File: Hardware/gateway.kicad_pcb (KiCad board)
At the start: 2 copper layers, 65 x 56 mm, 27 parts, among them J0 Raspberry_Pi_2_3_40HAT, J1 CONN_01X02, J2 Conn_Coaxial, J3 Conn_Coaxial, U0 CAT24C32, U0a1 DRF1278F, U0b1 XL1278-SMT, U0c1 RFM9xW-xxxS2, U1a1 DRF1278F, U1b1 XL1278-SMT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

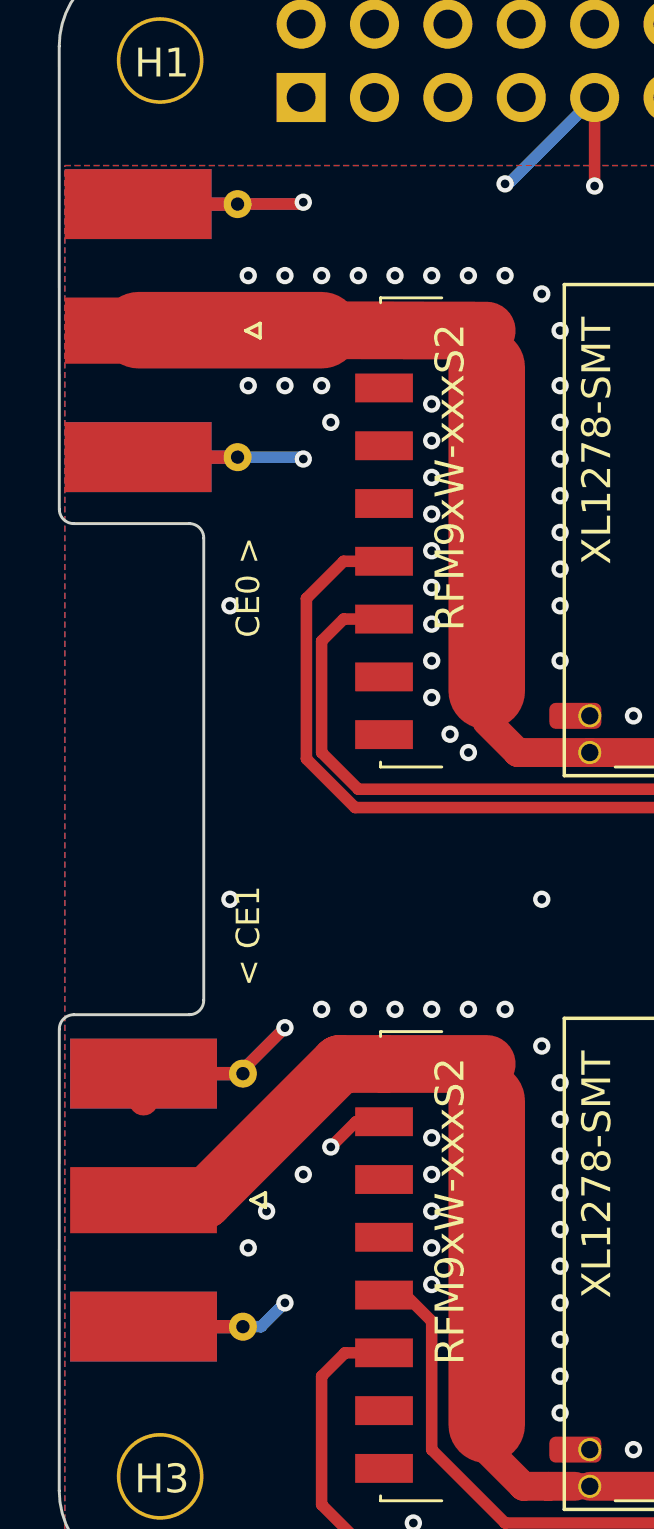
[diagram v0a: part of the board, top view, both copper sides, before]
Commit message: Fix antenna ground connections
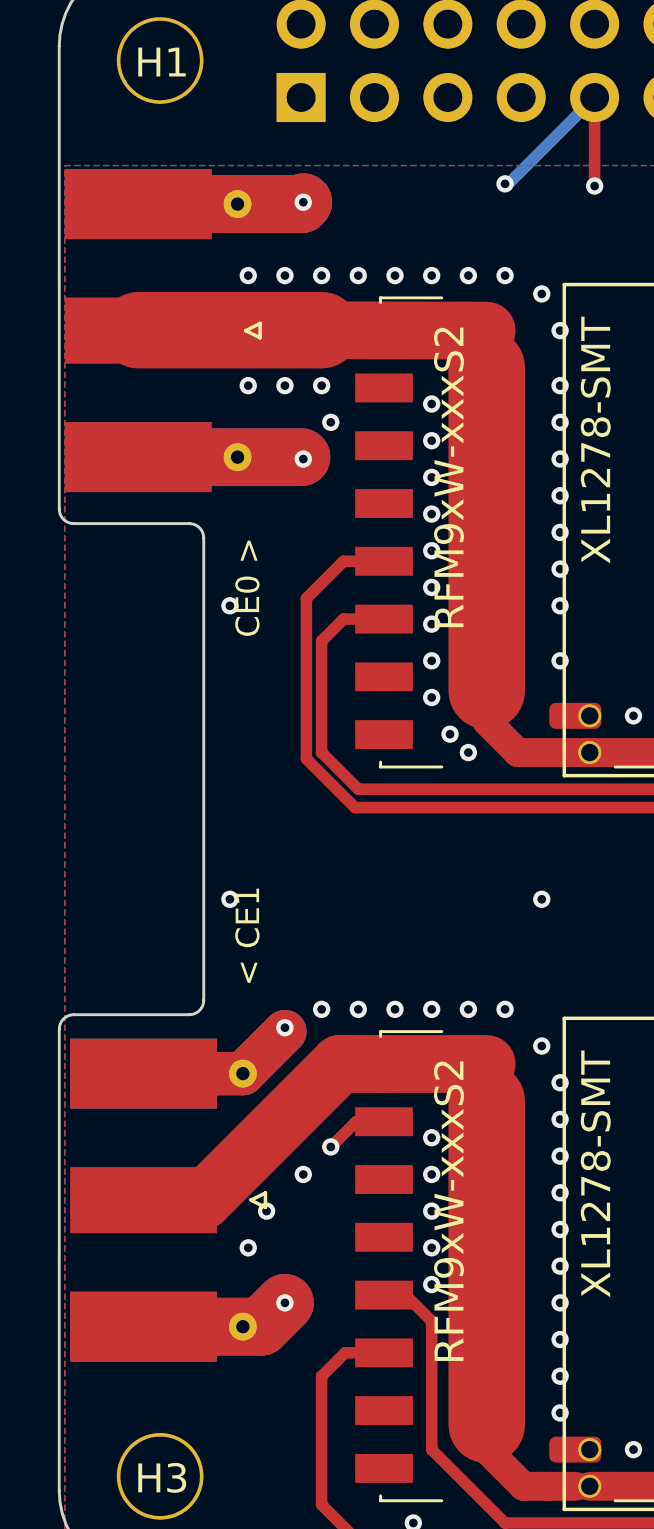
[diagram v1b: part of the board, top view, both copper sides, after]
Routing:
- net GND: track 56.1 -> 86.3 mm
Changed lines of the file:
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@@
     (thickness 1.6002)
     (drawings 32)
-    (tracks 431)
+    (tracks 436)
     (zones 0)
     (modules 27)
@@
   )
   (setup
-    (last_trace_width 0.6)
+    (last_trace_width 0.127)
     (user_trace_width 0.15)
     (user_trace_width 0.2)
@@
     (visible_elements 7FFFFE3F)
     (pcbplotparams
-      (layerselection 0x010f8_80000007)
+      (layerselection 0x010f0_ffffffff)
       (usegerberextensions false)
       (usegerberattributes false)
@@
       (plotinvisibletext false)
       (padsonsilk true)
-      (subtractmaskfromsilk false)
+      (subtractmaskfromsilk true)
       (outputformat 1)
       (mirror false)
       (drillshape 0)
       (scaleselection 1)
-      (outputdirectory "prod"))
+      (outputdirectory "Gerber/"))
   )
   (net 0 "")
@@
   (gr_line (start 81.546356 116.817611) (end 140.546356 116.817611) (layer Edge.Cuts) (width 0.1))
   (gr_arc (start 140.546356 113.817611) (end 140.546356 116.817611) (angle -89.9) (layer Edge.Cuts) (width 0.1))
-  (segment (start 81.48 100.315) (end 81.465 100.33) (width 1) (layer Front) (net 1) (status 30))
   (segment (start 105.79 113.045) (end 104.155 113.045) (width 0.4) (layer Front) (net 1) (status 10))
   (segment (start 103.505 112.395) (end 102.381 112.395) (width 0.4) (layer Front) (net 1) (status 20))
@@
   (via (at 86.995 78.105) (size 0.6) (drill 0.3) (layers Front Back) (net 1))
   (via (at 86.36 97.79) (size 0.6) (drill 0.3) (layers Front Back) (net 1))
-  (segment (start 84.905 99.245) (end 86.36 97.79) (width 0.4) (layer Front) (net 1) (status 10))
-  (segment (start 84.905 99.379) (end 84.905 99.245) (width 0.4) (layer Front) (net 1) (status 30))
-  (segment (start 86.93 69.28) (end 86.995 69.215) (width 0.4) (layer Back) (net 1))
-  (segment (start 84.72 69.28) (end 86.93 69.28) (width 0.4) (layer Back) (net 1) (status 10))
-  (segment (start 86.93 78.04) (end 86.995 78.105) (width 0.4) (layer Back) (net 1))
-  (segment (start 84.72 78.04) (end 86.93 78.04) (width 0.4) (layer Back) (net 1) (status 10))
-  (segment (start 84.455 99.379) (end 84.771 99.379) (width 0.4) (layer Back) (net 1) (status 30))
-  (segment (start 84.905 99.245) (end 86.36 97.79) (width 0.4) (layer Back) (net 1) (status 10))
-  (segment (start 84.905 99.379) (end 84.905 99.245) (width 0.4) (layer Back) (net 1) (status 30))
-  (segment (start 84.72 69.28) (end 86.93 69.28) (width 0.4) (layer Front) (net 1) (status 10))
-  (segment (start 81.465 99.379) (end 84.905 99.379) (width 0.4) (layer Front) (net 1) (status 30))
+  (segment (start 84.72 69.28) (end 86.93 69.28) (width 2) (layer Back) (net 1) (status 10))
+  (segment (start 81.465 99.379) (end 84.905 99.379) (width 1.5) (layer Front) (net 1) (status 30))
   (via (at 93.98 68.58) (size 0.6) (drill 0.3) (layers Front Back) (net 1))
   (segment (start 94.09 68.58) (end 93.98 68.58) (width 0.4) (layer Back) (net 1))
@@
   (segment (start 105.79 99.045) (end 106.06 99.045) (width 0.4) (layer Front) (net 1) (status 30))
   (segment (start 117.4 65.965) (end 117.4 65.59) (width 0.4) (layer Back) (net 1) (status 30))
-  (segment (start 84.905 108.139) (end 85.536 108.139) (width 0.4) (layer Back) (net 1) (status 10))
   (segment (start 135.18 65.59) (end 137.795 68.205) (width 0.4) (layer Front) (net 1) (status 10))
   (segment (start 117.4 65.59) (end 117.4 68.505) (width 0.4) (layer Front) (net 1) (status 10))
@@
   (segment (start 112.13 99.695) (end 110.49 99.695) (width 0.4) (layer Front) (net 1) (status 10))
   (segment (start 88.82 101.045) (end 87.9475 101.9175) (width 0.4) (layer Front) (net 1) (status 10))
-  (segment (start 85.536 108.139) (end 86.36 107.315) (width 0.4) (layer Back) (net 1))
   (segment (start 97.08 65.59) (end 97.08 68.655) (width 0.4) (layer Front) (net 1) (status 10))
   (segment (start 137.795 68.205) (end 137.795 68.58) (width 0.4) (layer Front) (net 1))
@@
   (via (at 90.805 114.935) (size 0.6) (drill 0.3) (layers Front Back) (net 1))
   (via (at 116.205 104.14) (size 0.6) (drill 0.3) (layers Front Back) (net 1))
+  (segment (start 86.93 78.04) (end 86.995 78.105) (width 0.127) (layer Front) (net 1))
+  (segment (start 81.28 78.04) (end 86.93 78.04) (width 2) (layer Front) (net 1))
+  (segment (start 86.93 69.28) (end 86.995 69.215) (width 2) (layer Front) (net 1))
+  (segment (start 81.28 69.28) (end 86.93 69.28) (width 2) (layer Front) (net 1))
+  (segment (start 85.536 108.139) (end 86.36 107.315) (width 2) (layer Front) (net 1))
+  (segment (start 81.465 108.139) (end 85.536 108.139) (width 2) (layer Front) (net 1))
+  (segment (start 85.536 108.139) (end 86.36 107.315) (width 2) (layer Back) (net 1))
+  (segment (start 81.465 108.139) (end 85.536 108.139) (width 2) (layer Back) (net 1))
+  (segment (start 81.465 99.379) (end 84.905 99.379) (width 1.5) (layer Back) (net 1))
+  (segment (start 86.36 97.924) (end 86.36 97.79) (width 0.127) (layer Back) (net 1))
+  (segment (start 84.905 99.379) (end 86.36 97.924) (width 1.5) (layer Back) (net 1))
+  (segment (start 86.36 97.924) (end 86.36 97.79) (width 0.127) (layer Front) (net 1))
+  (segment (start 84.905 99.379) (end 86.36 97.924) (width 1.5) (layer Front) (net 1))
+  (segment (start 86.93 78.04) (end 86.995 78.105) (width 0.127) (layer Back) (net 1))
+  (segment (start 81.28 78.04) (end 86.93 78.04) (width 2) (layer Back) (net 1))
+  (segment (start 86.93 69.28) (end 86.995 69.215) (width 2) (layer Back) (net 1))
+  (segment (start 81.28 69.28) (end 86.93 69.28) (width 2) (layer Back) (net 1))
   (segment (start 119.94 65.59) (end 119.94 67.235) (width 0.4) (layer Back) (net 2) (status 10))
   (segment (start 121.287009 68.582009) (end 132.496705 68.582009) (width 0.4) (layer Back) (net 2))
@@
       )
     )
+  )
+  (zone (net 0) (net_name "") (layer Front) (hatch edge 0.508)
+    (connect_pads (clearance 0.2))
+    (min_thickness 0.254)
+    (keepout (tracks allowed) (vias allowed) (copperpour not_allowed))
+    (fill (arc_segments 32) (thermal_gap 0.508) (thermal_bridge_width 0.508))
+    (polygon
+      (pts
+        (xy 84.455 76.835) (xy 78.74 76.835) (xy 78.74 70.485) (xy 84.455 70.485)
+      )
+    )
+  )
+  (zone (net 0) (net_name "") (layer Front) (hatch edge 0.508)
+    (connect_pads (clearance 0.2))
+    (min_thickness 0.254)
+    (keepout (tracks allowed) (vias allowed) (copperpour not_allowed))
+    (fill (arc_segments 32) (thermal_gap 0.508) (thermal_bridge_width 0.508))
+    (polygon
+      (pts
+        (xy 84.0105 106.934) (xy 78.9305 106.934) (xy 78.9305 100.584) (xy 84.0105 100.584)
+      )
+    )

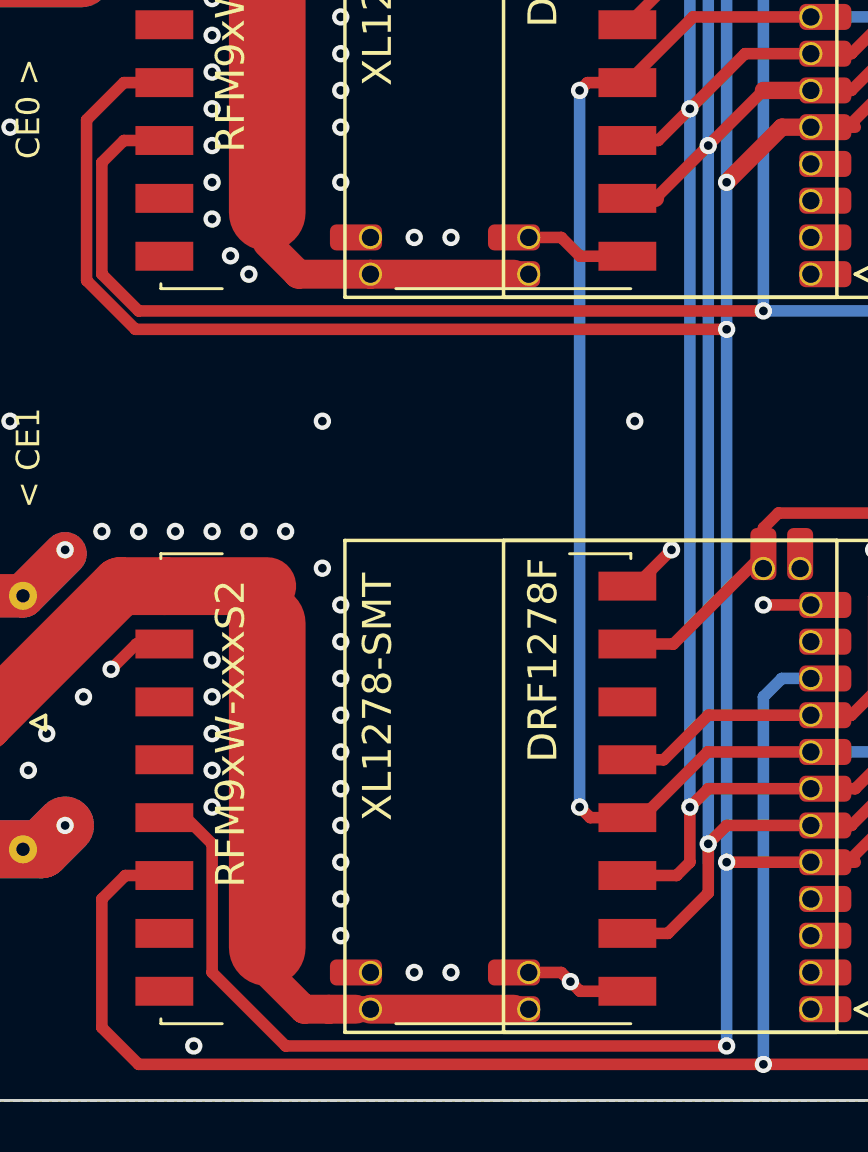
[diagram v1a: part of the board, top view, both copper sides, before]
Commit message: Fix more grounds.
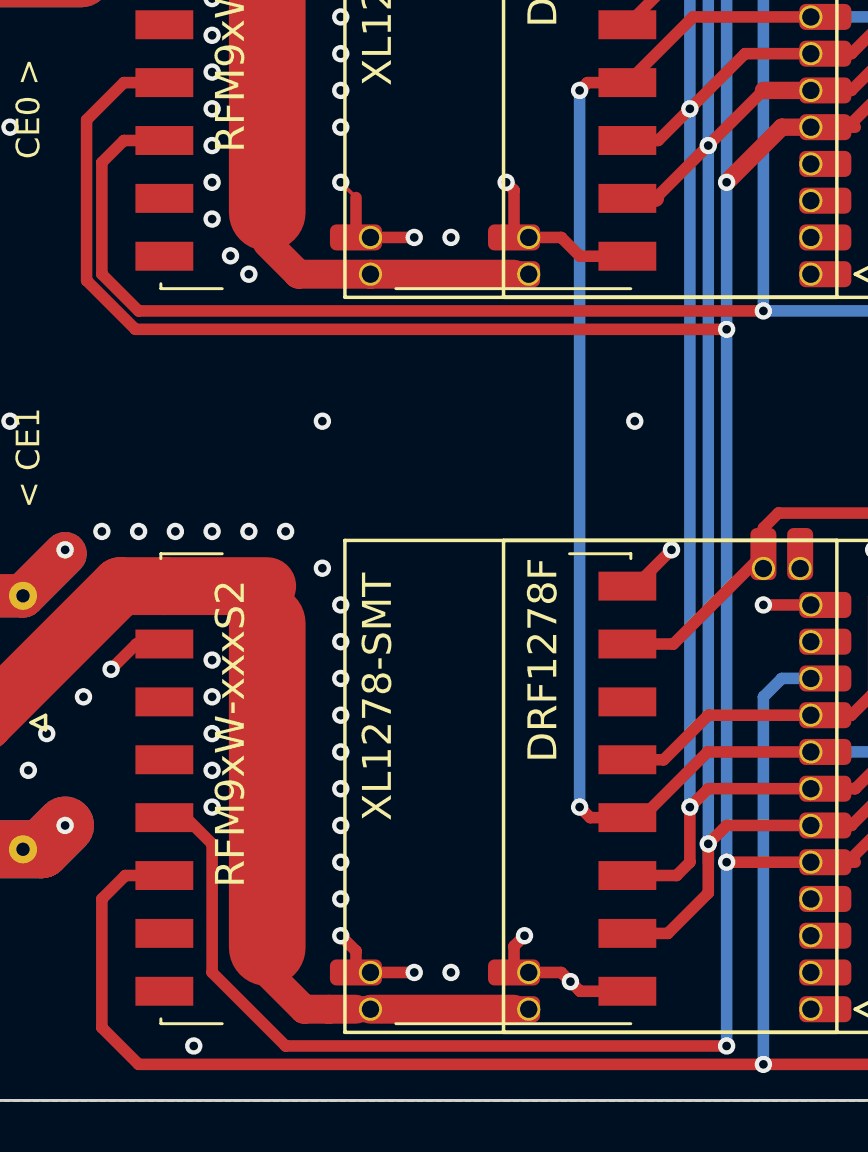
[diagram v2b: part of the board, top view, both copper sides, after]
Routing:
- net GND: track 86.3 -> 97.4 mm, vias 90 -> 92
